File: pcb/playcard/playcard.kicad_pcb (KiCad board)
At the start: 2 copper layers, 9 parts, among them SW1 SW_MEC_5E, SW2 SW_MEC_5E, SW3 SW_MEC_5E, SW4 SW_MEC_5E, SW5 SW_MEC_5E, SW6 SW_MEC_5E, U1 BlackPill_Part_Like_SWD_Break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, U3 2.4_TFT_ILI9341, U4 ESP32-S3-ZERO

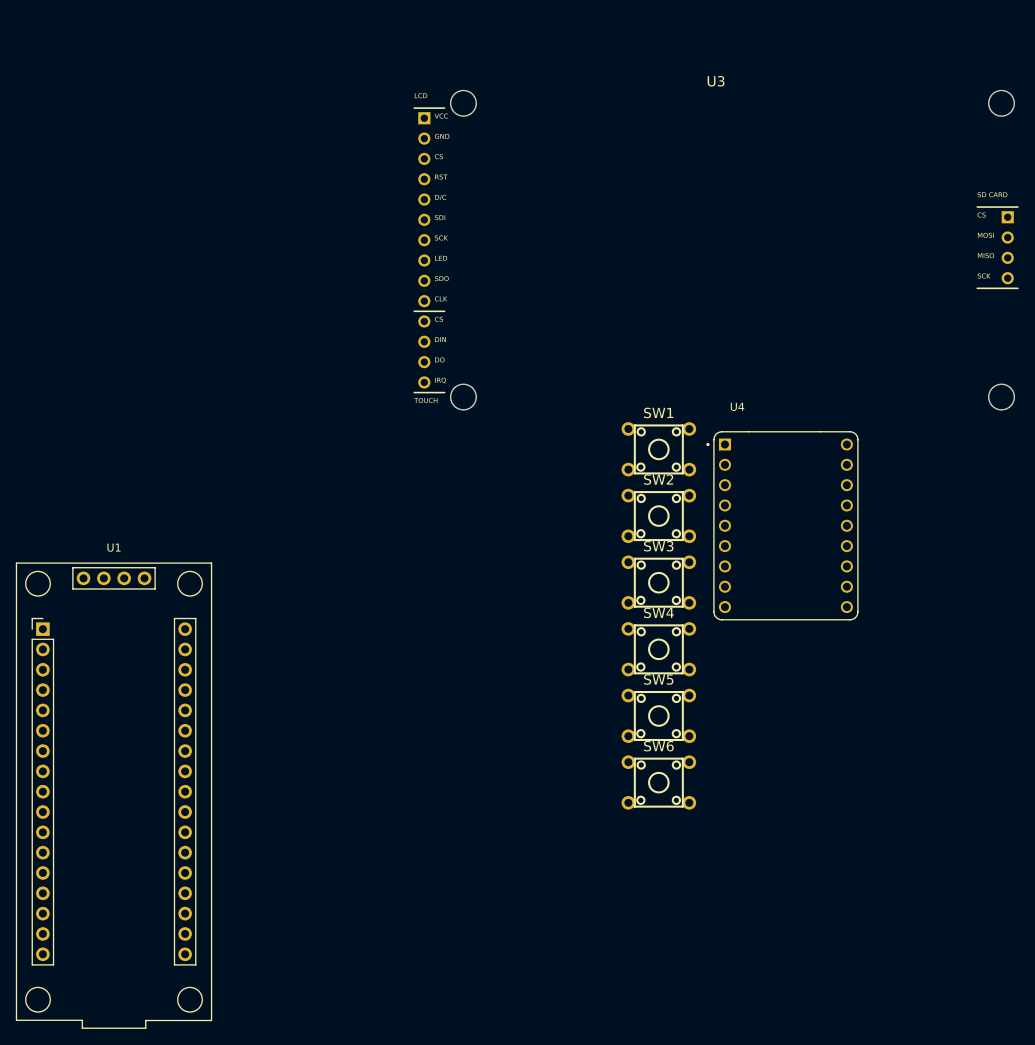
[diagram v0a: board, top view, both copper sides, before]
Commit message: updated pcb and readme
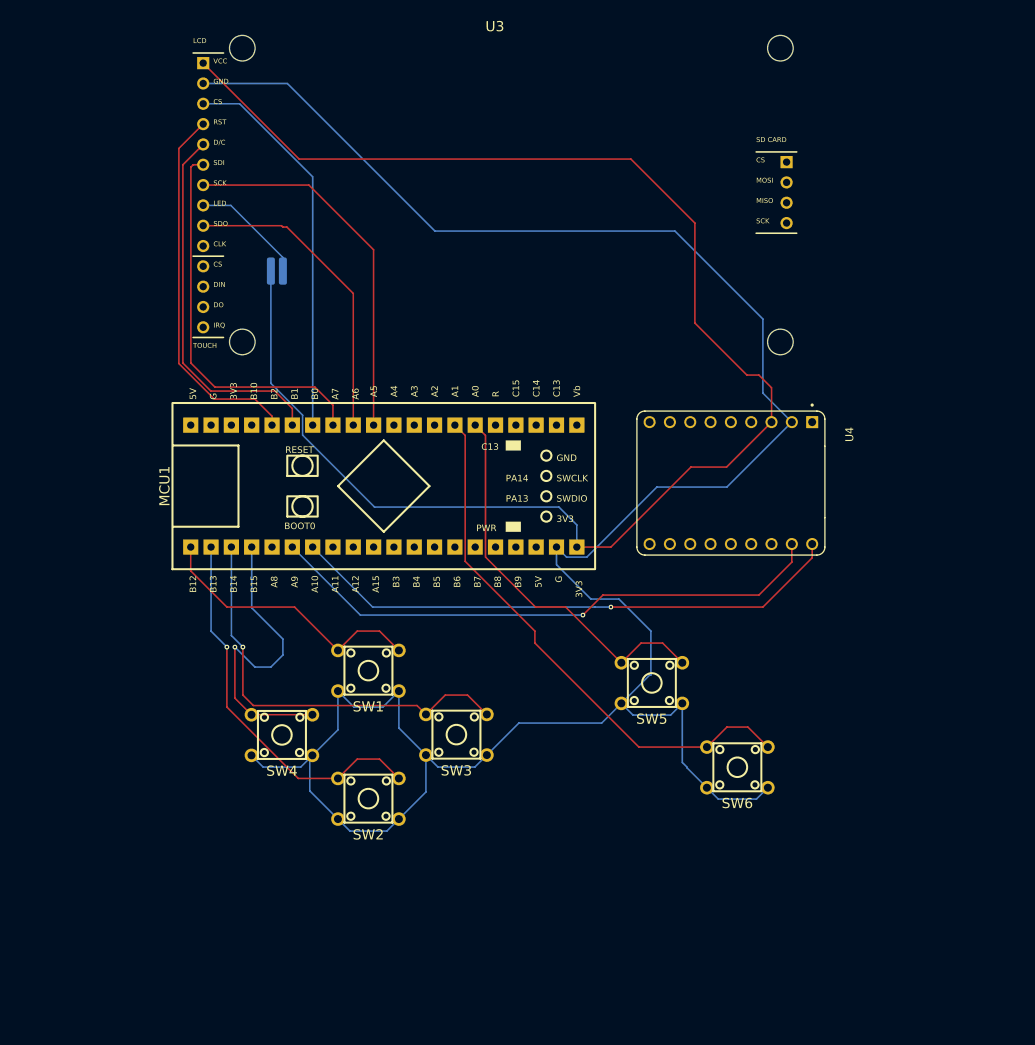
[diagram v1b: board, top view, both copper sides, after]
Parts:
- removed U1: BlackPill_Part_Like_SWD_Breakout, MCU_personal:BlackPill_SWD_2
- added MCU1: BLACK PILL V3 STM32F411, MCU_personal:BLACK PILL V3, F.Cu at (98.1, 102.4)
- added R1: 47K, Resistor_SMD:R_0612_1632Metric, B.Cu at (84.8, 75.5)
- moved SW2 42.2 mm to (99.2, 138.4), turned to 180 degrees
- moved SW4 41.4 mm to (88.4, 130.5), turned to 180 degrees
- moved SW1 37.2 mm to (99.2, 122.4), turned to 180 degrees
- moved U3 28.5 mm to (75.5, 49.5)
- moved SW3 23.3 mm to (110.2, 130.4), turned to 180 degrees
- moved SW6 17.7 mm to (145.3, 134.5), turned to 180 degrees
- moved SW5 11.4 mm to (134.6, 124.0), turned to 180 degrees
- moved U4 8.71 mm to (141.5, 102.0), turned to -90 degrees
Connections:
- net Net-(SW1-A) renamed /UP
- SW2 pad 3: unconnected-(SW2-K-Pad3) -> /DOWN
- SW2 pad 4: unconnected-(SW2-A-Pad4) -> /DOWN
- SW3 pad 3: unconnected-(SW3-K-Pad3) -> /RIGHT
- SW3 pad 4: unconnected-(SW3-A-Pad4) -> /RIGHT
- SW4 pad 3: unconnected-(SW4-K-Pad3) -> /LEFT
- SW4 pad 4: unconnected-(SW4-A-Pad4) -> /LEFT
- SW5 pad 3: unconnected-(SW5-K-Pad3) -> /A
- SW5 pad 4: unconnected-(SW5-A-Pad4) -> /A
- SW6 pad 3: unconnected-(SW6-K-Pad3) -> /B
- SW6 pad 4: unconnected-(SW6-A-Pad4) -> /B
- U3 pad 3: unconnected-(U3-CS-Pad3) -> /CS
- U3 pad 4: unconnected-(U3-RESET-Pad4) -> /RST
- U3 pad 5: unconnected-(U3-D/C-Pad5) -> /D/C
- U3 pad 6: unconnected-(U3-SDI_(MOSI)-Pad6) -> /SDI
- U3 pad 7: unconnected-(U3-SCK-Pad7) -> /SCK
- U3 pad 8: unconnected-(U3-LED-Pad8) -> Net-(U3-LED)
- U3 pad 9: unconnected-(U3-SDO_(MISO)-Pad9) -> /SDO
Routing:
- net GND: track 0.00 -> 284.0 mm
- net VCC: track 0.00 -> 194.1 mm
- net TX1: track 0.00 -> 71.0 mm, vias 0 -> 1
- net RX1: track 0.00 -> 69.8 mm, vias 0 -> 1
- net /B: track 0.00 -> 68.0 mm
- net /RIGHT: track 0.00 -> 52.6 mm, vias 0 -> 1
- net /A: track 0.00 -> 49.1 mm
- net /SDI: track 0.00 -> 48.6 mm
- net /CS: track 0.00 -> 48.5 mm
- net /DOWN: track 0.00 -> 48.0 mm, vias 0 -> 1
- net /RST: track 0.00 -> 46.7 mm
- net /SCK: track 0.00 -> 46.6 mm
- net /D/C: track 0.00 -> 46.5 mm
- net /LEFT: track 0.00 -> 39.7 mm, vias 0 -> 1
- net /SDO: track 0.00 -> 38.7 mm
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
